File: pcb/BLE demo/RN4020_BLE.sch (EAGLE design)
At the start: 20 parts, among them U1 PIC18LF25K50-I/SO, U2 TC1262_VDB

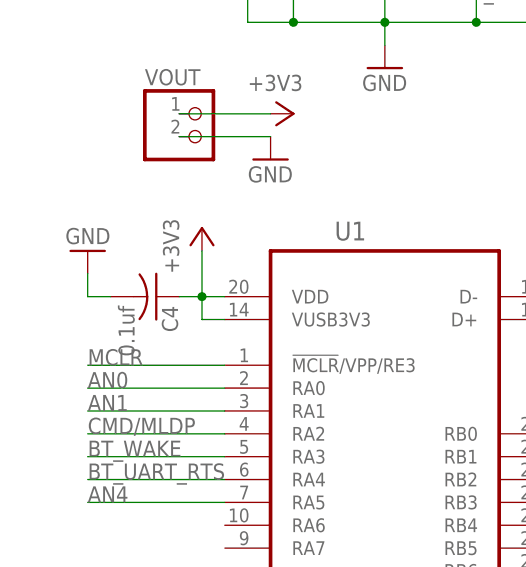
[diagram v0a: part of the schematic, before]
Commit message: fixed BLE PCB, removed version from file name
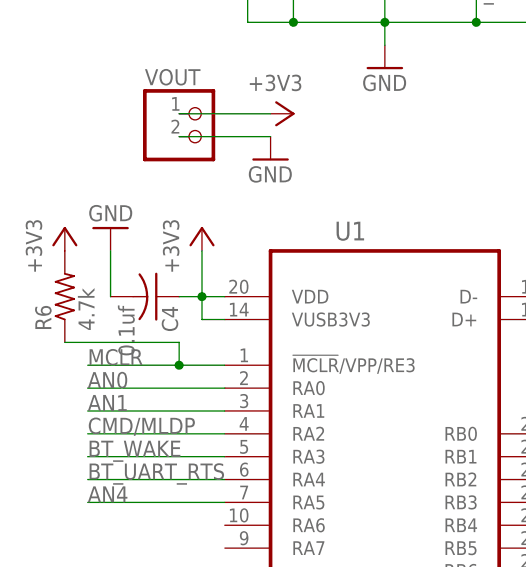
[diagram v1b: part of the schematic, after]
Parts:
- added R6: 4.7k, resistor:R-US_R1206
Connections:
- net +3V3: now also R6.2
- net MCLR: now also R6.1
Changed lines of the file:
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@@
 <?xml version="1.0" encoding="utf-8"?>
 <!DOCTYPE eagle SYSTEM "eagle.dtd">
-<eagle version="7.4.0">
+<eagle version="7.5.0">
 <drawing>
 <settings>
@@
 <part name="+3V7" library="supply1" deviceset="+3V3" device=""/>
 <part name="GND11" library="supply1" deviceset="GND" device=""/>
+<part name="R6" library="resistor" deviceset="R-US_" device="R1206" value="4.7k"/>
+<part name="+3V8" library="supply1" deviceset="+3V3" device=""/>
 </parts>
 <sheets>
@@
 <instance part="A2D" gate="A" x="154.94" y="-15.24"/>
 <instance part="C4" gate="G$1" x="35.56" y="25.4" rot="R270"/>
-<instance part="GND10" gate="1" x="27.94" y="30.48" rot="R180"/>
+<instance part="GND10" gate="1" x="30.48" y="33.02" rot="R180"/>
 <instance part="VOUT" gate="G$1" x="40.64" y="43.18"/>
 <instance part="+3V7" gate="G$1" x="50.8" y="45.72" rot="R270"/>
 <instance part="GND11" gate="1" x="48.26" y="40.64"/>
+<instance part="R6" gate="G$1" x="25.4" y="25.4" rot="R90"/>
+<instance part="+3V8" gate="G$1" x="25.4" y="33.02"/>
 </instances>
 <busses>
@@
 <segment>
 <pinref part="U1" gate="A" pin="!MCLR!/VPP/RE3"/>
-<wire x1="43.18" y1="17.78" x2="27.94" y2="17.78" width="0.1524" layer="91"/>
+<wire x1="43.18" y1="17.78" x2="38.1" y2="17.78" width="0.1524" layer="91"/>
 <label x="27.94" y="17.78" size="1.778" layer="95"/>
+<wire x1="38.1" y1="17.78" x2="27.94" y2="17.78" width="0.1524" layer="91"/>
+<wire x1="38.1" y1="17.78" x2="38.1" y2="20.32" width="0.1524" layer="91"/>
+<junction x="38.1" y="17.78"/>
+<pinref part="R6" gate="G$1" pin="1"/>
+<wire x1="38.1" y1="20.32" x2="25.4" y2="20.32" width="0.1524" layer="91"/>
 </segment>
 <segment>
@@
 <pinref part="C4" gate="G$1" pin="2"/>
 <pinref part="GND10" gate="1" pin="GND"/>
-<wire x1="30.48" y1="25.4" x2="27.94" y2="25.4" width="0.1524" layer="91"/>
-<wire x1="27.94" y1="25.4" x2="27.94" y2="27.94" width="0.1524" layer="91"/>
+<wire x1="30.48" y1="25.4" x2="30.48" y2="30.48" width="0.1524" layer="91"/>
 </segment>
 <segment>
@@
 <pinref part="+3V7" gate="G$1" pin="+3V3"/>
 </segment>
-</net>
+<segment>
+<pinref part="R6" gate="G$1" pin="2"/>
+<pinref part="+3V8" gate="G$1" pin="+3V3"/>
+</segment>
+</net>
